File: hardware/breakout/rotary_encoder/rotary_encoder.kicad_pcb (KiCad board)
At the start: 2 copper layers, 34 x 28 mm, 4 parts, among them J1 Conn_01x04_Pin, SW1 RotaryEncoder_Switch

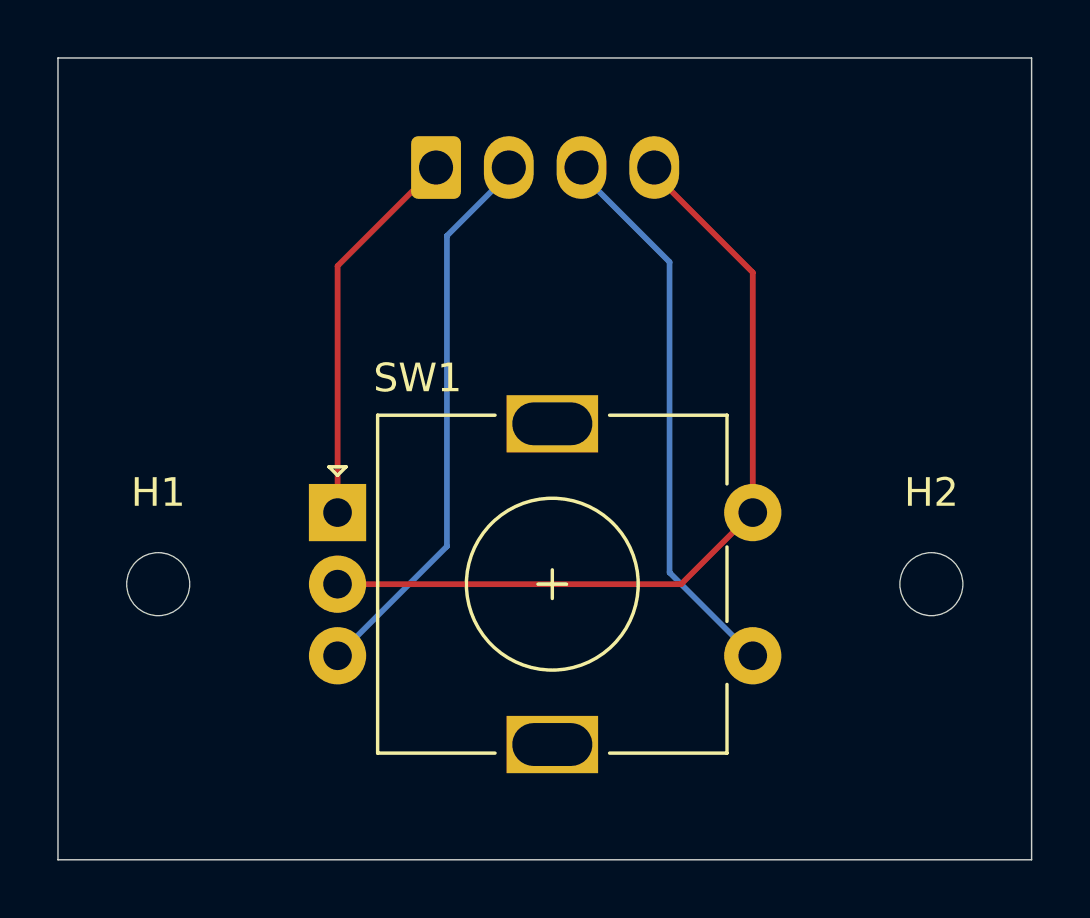
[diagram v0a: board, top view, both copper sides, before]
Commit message: center the knob
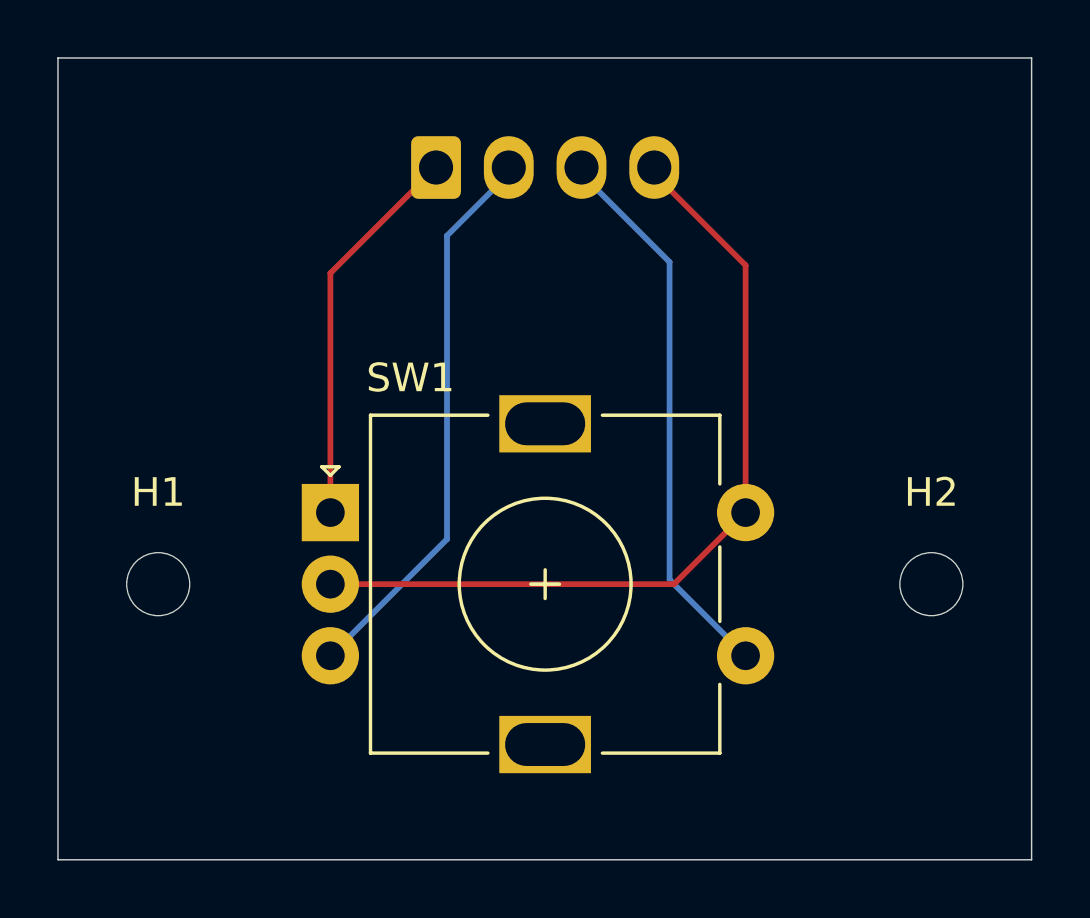
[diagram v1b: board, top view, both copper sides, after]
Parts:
- moved SW1 0.25 mm to (130.8, 91.4)
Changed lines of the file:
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@@
 	(footprint "Rotary_Encoder:RotaryEncoder_Alps_EC11E-Switch_Vertical_H20mm"
 		(layer "F.Cu")
-		(at 131.055 91.375)
+		(at 130.805 91.375)
 		(descr "Alps rotary encoder, EC12E... with switch, vertical shaft, http://www.alps.com/prod/info/E/HTML/Encoder/Incremental/EC11/EC11E15204A3.html")
 		(tags "rotary encoder")
@@
 		)
 		(embedded_fonts no)
-		(model "${KIPRJMOD}/import/LIB_EC11E183440C/EC11E183440C/3D/EC11E183440C.stp"
+		(model "/home/martin/Downloads/LIB_EC11E183440C/EC11E183440C/3D/EC11E183440C.stp"
 			(offset
 				(xyz 7.5 -2.5 3.5)
@@
 	(segment
 		(start 134.495 79.325)
-		(end 131.055 82.765)
+		(end 130.805 83.015)
 		(width 0.2)
 		(layer "F.Cu")
@@
 	)
 	(segment
-		(start 131.055 82.765)
-		(end 131.055 91.375)
+		(start 130.805 83.015)
+		(end 130.805 91.375)
 		(width 0.2)
 		(layer "F.Cu")
@@
 	)
 	(segment
+		(start 134.875 92.305)
+		(end 130.805 96.375)
+		(width 0.2)
+		(layer "B.Cu")
+		(net "Net-(J1-Pin_2)")
+	)
+	(segment
+		(start 134.875 81.71)
+		(end 134.875 92.305)
+		(width 0.2)
+		(layer "B.Cu")
+		(net "Net-(J1-Pin_2)")
+	)
+	(segment
 		(start 137.035 79.55)
 		(end 134.875 81.71)
@@
 	)
 	(segment
-		(start 131.055 96.375)
-		(end 134.875 92.555)
-		(width 0.2)
-		(layer "B.Cu")
-		(net "Net-(J1-Pin_2)")
-	)
-	(segment
-		(start 134.875 92.555)
-		(end 134.875 81.71)
-		(width 0.2)
-		(layer "B.Cu")
-		(net "Net-(J1-Pin_2)")
+		(start 145.305 91.375)
+		(end 142.805 93.875)
+		(width 0.2)
+		(layer "F.Cu")
+		(net "Net-(J1-Pin_4)")
+	)
+	(segment
+		(start 142.115 79.325)
+		(end 142.115 79.55)
+		(width 0.2)
+		(layer "F.Cu")
+		(net "Net-(J1-Pin_4)")
+	)
+	(segment
+		(start 145.305 82.74)
+		(end 145.305 91.375)
+		(width 0.2)
+		(layer "F.Cu")
+		(net "Net-(J1-Pin_4)")
+	)
+	(segment
+		(start 142.805 93.875)
+		(end 130.805 93.875)
+		(width 0.2)
+		(layer "F.Cu")
+		(net "Net-(J1-Pin_4)")
+	)
+	(segment
+		(start 142.115 79.55)
+		(end 145.305 82.74)
+		(width 0.2)
+		(layer "F.Cu")
+		(net "Net-(J1-Pin_4)")
 	)
 	(segment
@@
 	)
 	(segment
+		(start 142.65 82.625)
+		(end 142.65 93.72)
+		(width 0.2)
+		(layer "B.Cu")
+		(net "Net-(J1-Pin_3)")
+	)
+	(segment
+		(start 142.65 93.72)
+		(end 145.305 96.375)
+		(width 0.2)
+		(layer "B.Cu")
+		(net "Net-(J1-Pin_3)")
+	)
+	(segment
+		(start 145.4175 96.375)
+		(end 145.555 96.375)
+		(width 0.2)
+		(layer "B.Cu")
+		(net "Net-(J1-Pin_3)")
+	)
+	(segment
 		(start 139.575 79.55)
 		(end 142.65 82.625)
@@
 		(net "Net-(J1-Pin_3)")
 	)
-	(segment
-		(start 142.65 82.625)
-		(end 142.65 93.47)
-		(width 0.2)
-		(layer "B.Cu")
-		(net "Net-(J1-Pin_3)")
-	)
-	(segment
-		(start 142.65 93.47)
-		(end 145.555 96.375)
-		(width 0.2)
-		(layer "B.Cu")
-		(net "Net-(J1-Pin_3)")
-	)
-	(segment
-		(start 143.055 93.875)
-		(end 145.555 91.375)
-		(width 0.2)
-		(layer "F.Cu")
-		(net "Net-(J1-Pin_4)")
-	)
-	(segment
-		(start 131.055 93.875)
-		(end 143.055 93.875)
-		(width 0.2)
-		(layer "F.Cu")
-		(net "Net-(J1-Pin_4)")
-	)
-	(segment
-		(start 142.115 79.55)
-		(end 145.555 82.99)
-		(width 0.2)
-		(layer "F.Cu")
-		(net "Net-(J1-Pin_4)")
-	)
-	(segment
-		(start 145.555 91.375)
-		(end 145.555 82.99)
-		(width 0.2)
-		(layer "F.Cu")
-		(net "Net-(J1-Pin_4)")
-	)
-	(segment
-		(start 142.115 79.325)
-		(end 142.115 79.55)
-		(width 0.2)
-		(layer "F.Cu")
-		(net "Net-(J1-Pin_4)")
-	)
 	(embedded_fonts no)
